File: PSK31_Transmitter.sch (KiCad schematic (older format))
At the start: 38 parts

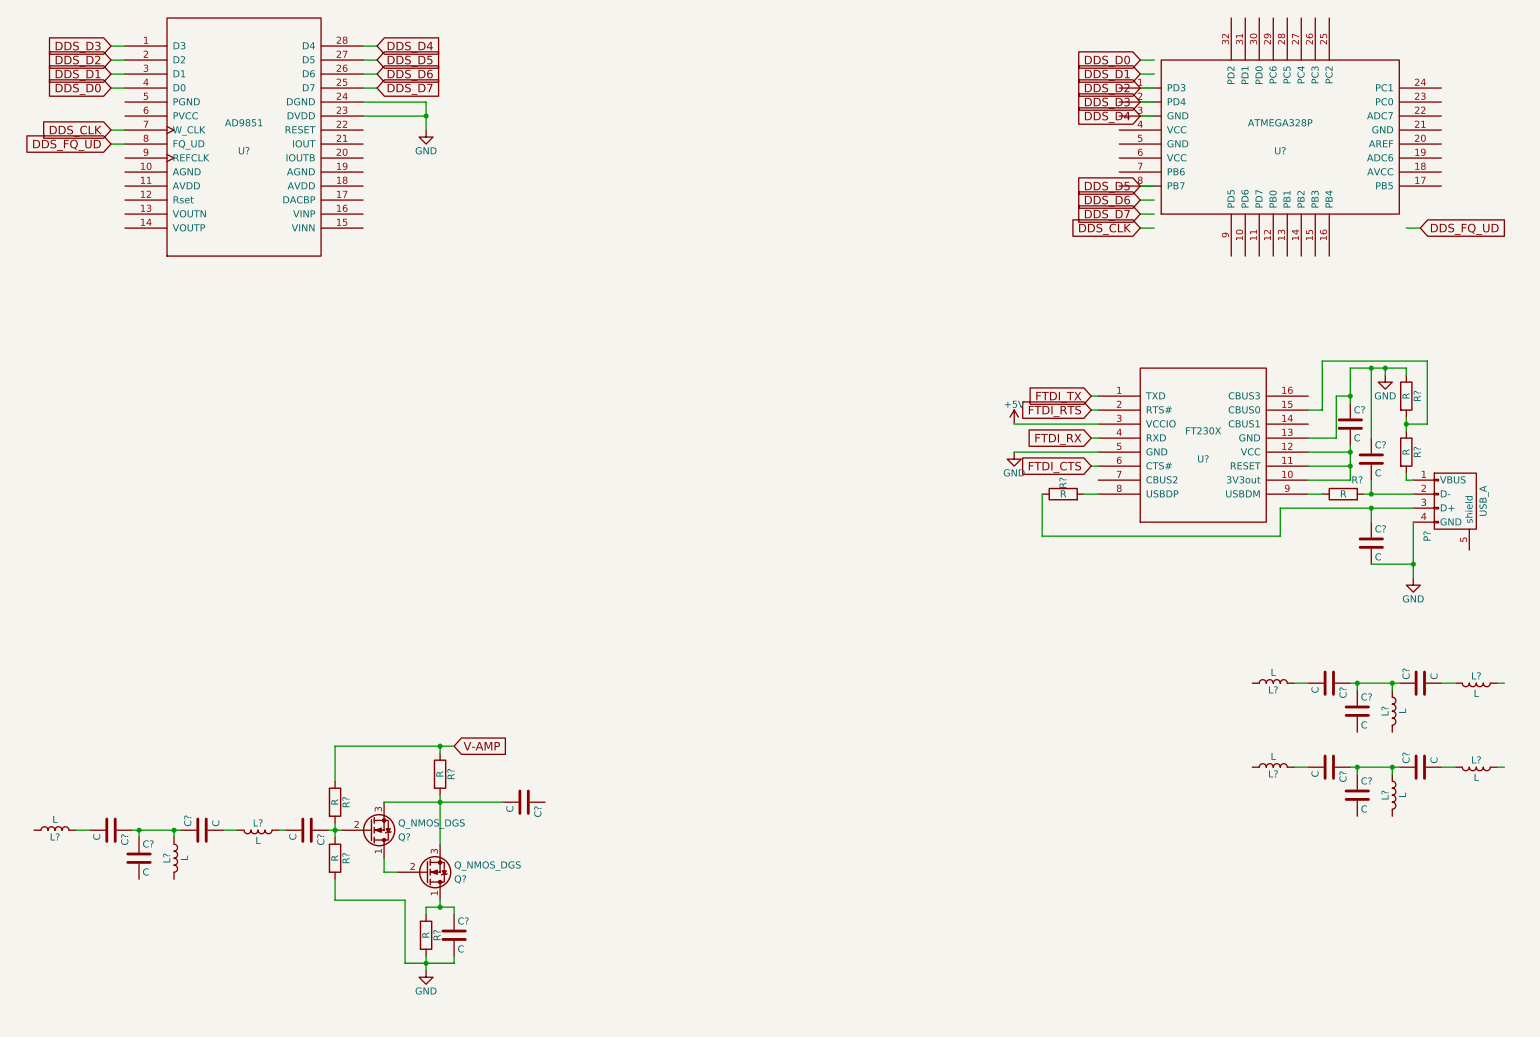
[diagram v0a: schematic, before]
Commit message: Add external circuitry for ftdi and dds.
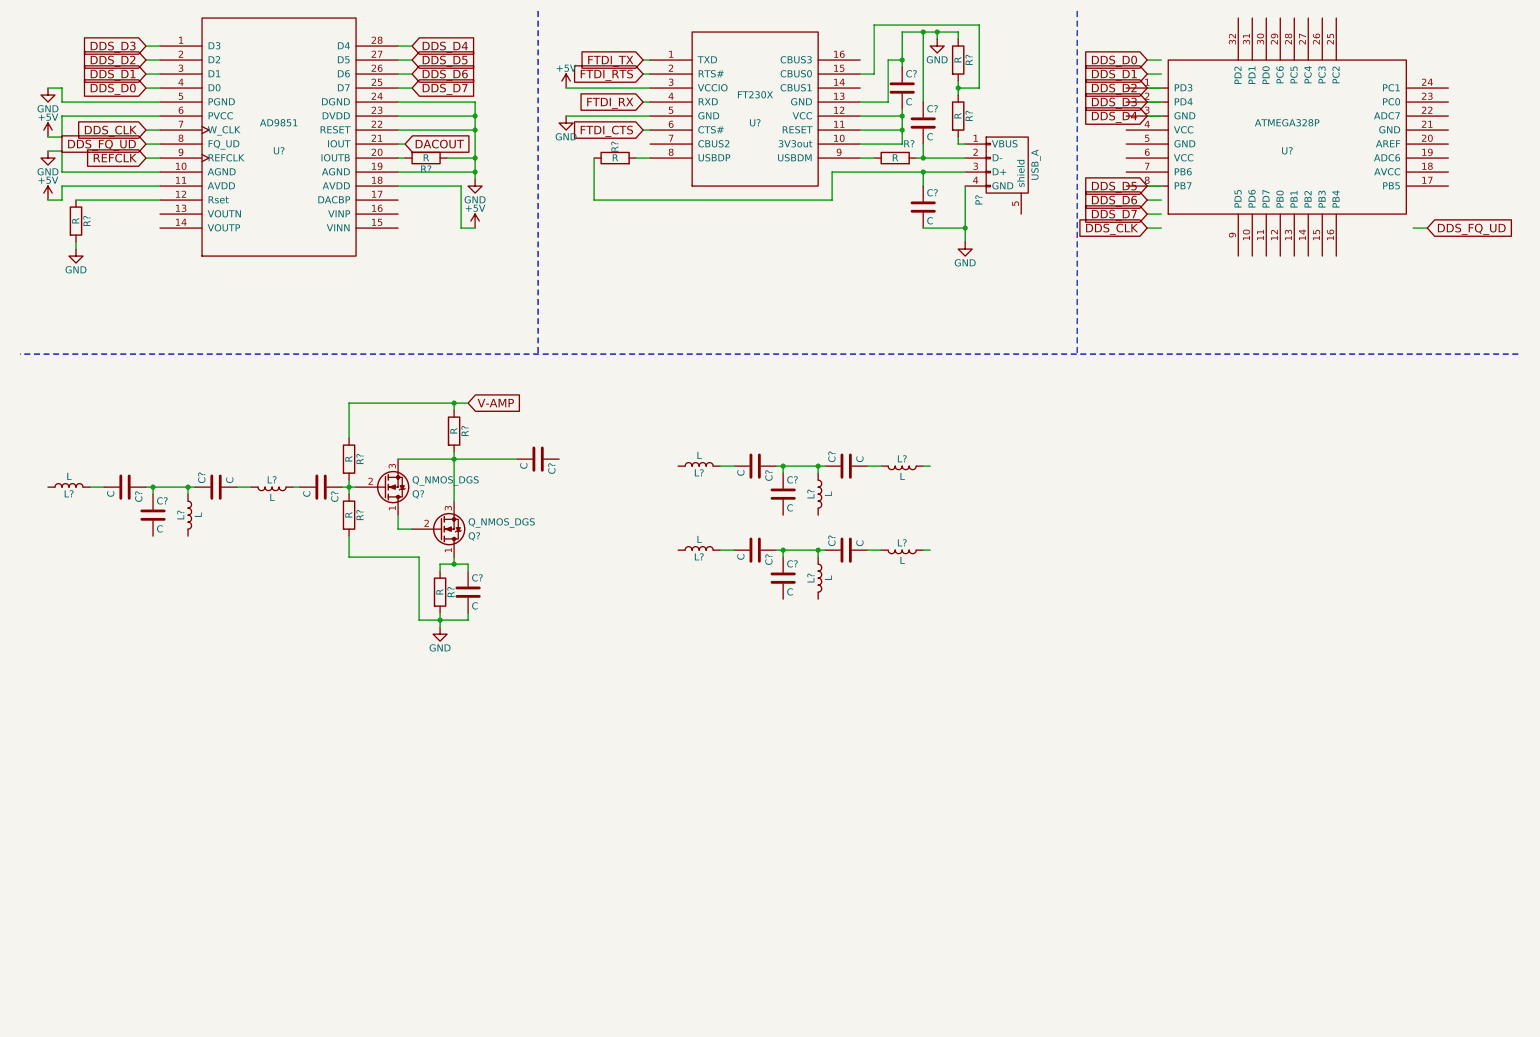
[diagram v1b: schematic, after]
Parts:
- added R? (x2): R, symbol R
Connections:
- net labels added: DACOUT, REFCLK
- wire segments 97 -> 120
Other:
- moved on the sheet: C?, L?, P?, Q?, R?, U?

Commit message: Add dac filter and dds reference clock
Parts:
- removed C? (x12): C, symbol C
- removed L? (x9): L, symbol L
- removed Q? (x2): Q_NMOS_DGS, symbol Q_NMOS_DGS
- removed R? (x4): R, symbol R
- added C? (x16): C, symbol C
- added L? (x4): L, symbol L
- added P?: CONN_01X02, symbol CONN_01X02
- added R?: R, symbol R
- added U?: TXETDDSANF-30.000000, MODULE, symbol TXETDDSANF-30.000000
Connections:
- net labels added: ISP_CLK, ISP_MISO, ISP_MOSI, ISP_RESET, RFOUT
- net labels removed: V-AMP
- wire segments 120 -> 128

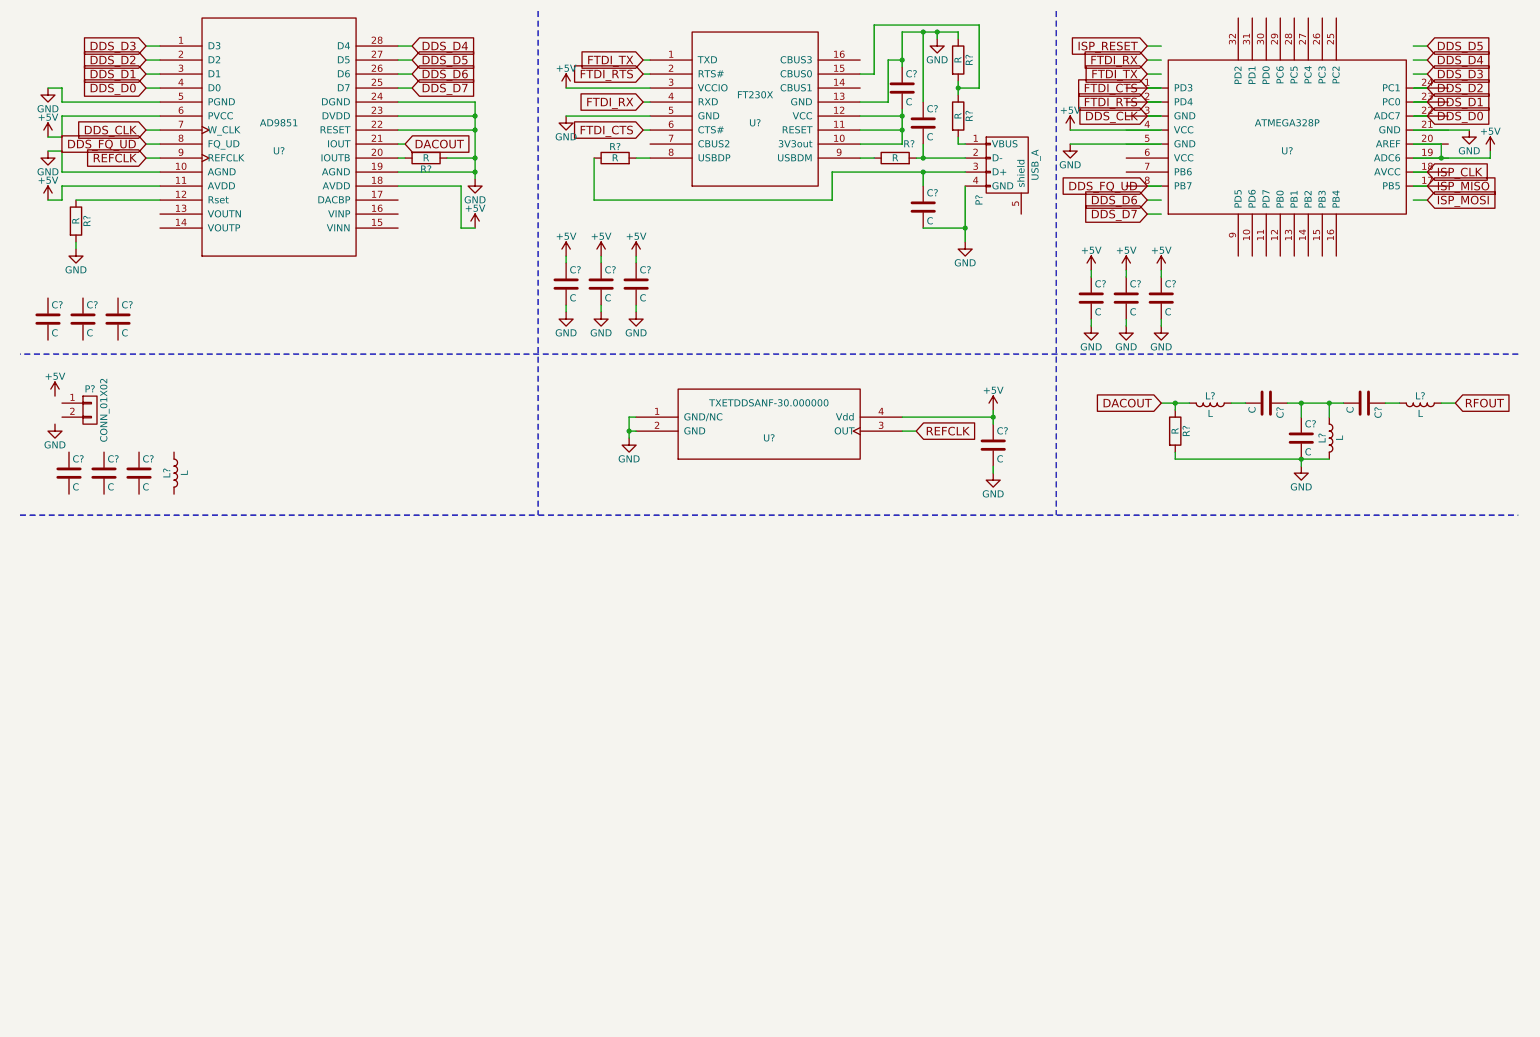
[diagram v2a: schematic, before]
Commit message: Add dds clock amplifer/filter and add dds output amplifier/filter
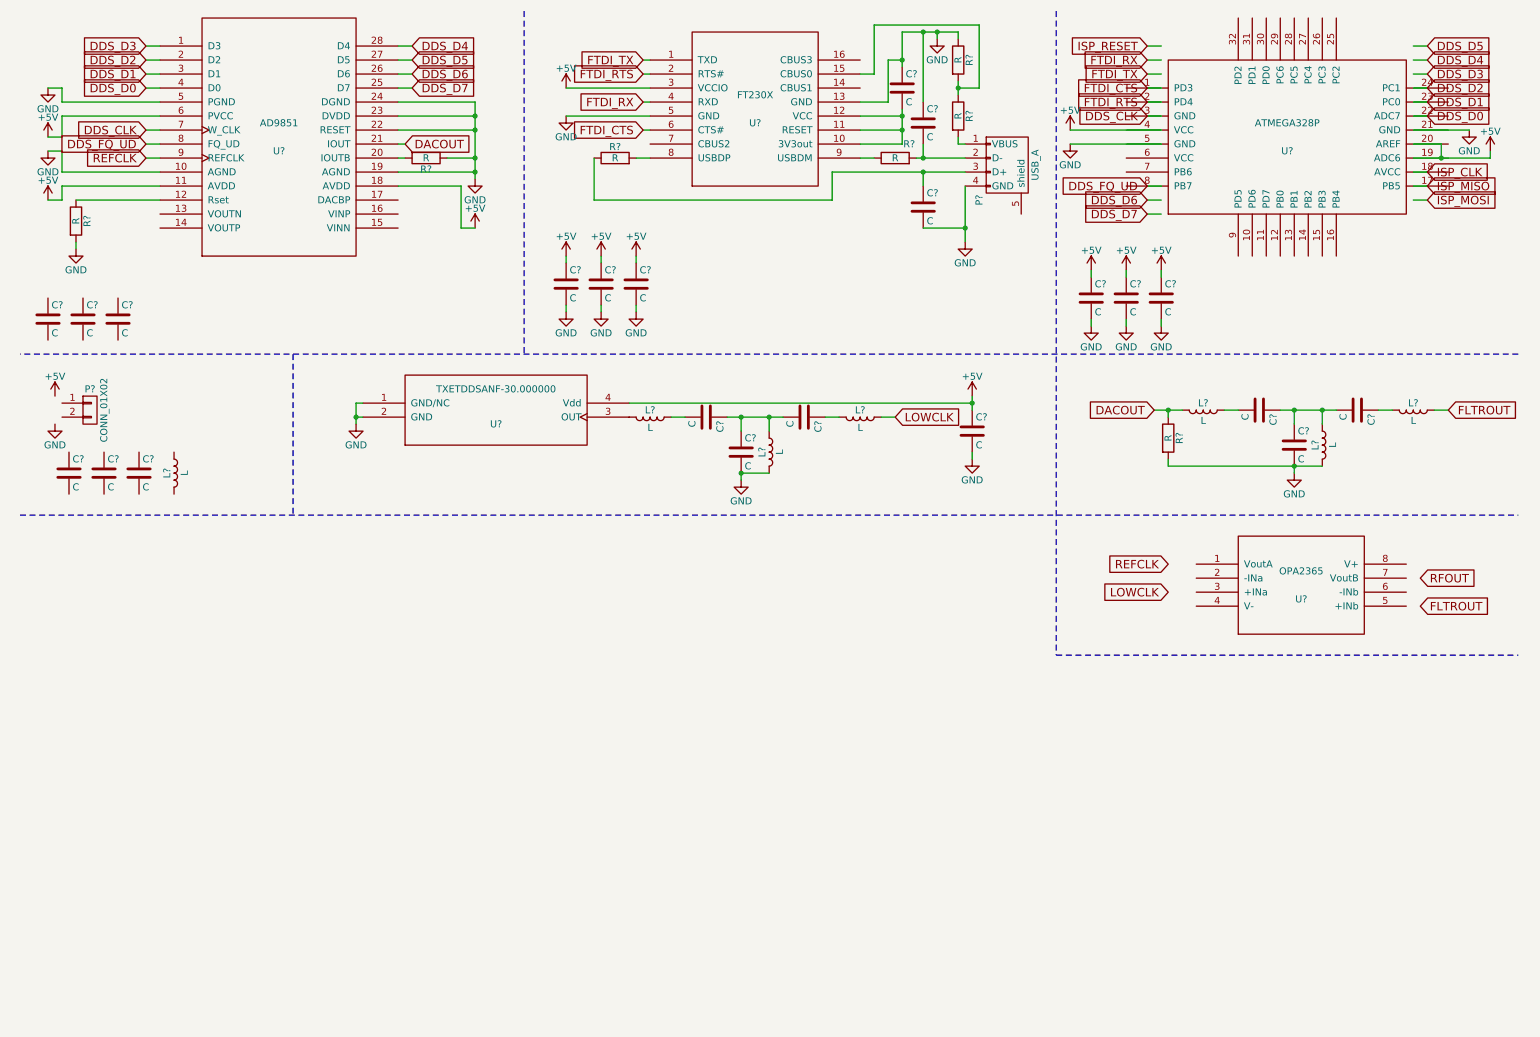
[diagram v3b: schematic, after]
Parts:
- added C? (x3): C, symbol C
- added L? (x3): L, symbol L
- added U?: OPA2365, MODULE, symbol OPA2365
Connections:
- net labels added: FLTROUT, LOWCLK
- wire segments 128 -> 135
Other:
- moved on the sheet: C?, L?, R?, U?

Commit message: update
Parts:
- removed C? (x19): C, symbol C
- removed L? (x7): L, symbol L
- removed P?: USB_A, symbol USB_A
- removed P?: CONN_01X02, symbol CONN_01X02
- removed R? (x5): R, symbol R
- removed U?: ATMEGA328P, MODULE, symbol ATMEGA328P
- removed U?: FT230X, MODULE, symbol FT230X
- added C1, C10, C11, C12, C13, C14, C16, C17, C19, C2, C21, C22, C23, C24, C25, C26, C27, C28, C29, C3, C30, C31, C32, C33, C4, C5, C6, C7, C8, C9: C, Capacitors_SMD:C_1206_HandSoldering, symbol C
- added L1, L2, L3, L4, L5, L6: L, Inductors_SMD:L_1206_Handsoldering, symbol L
- added P1: CONN_02X03, Pin_Headers:Pin_Header_Angled_2x03_Pitch2.54mm, symbol CONN_02X03
- added P2: CONN_01X04, Pin_Headers:Pin_Header_Angled_1x04_Pitch2.54mm, symbol CONN_01X04
- added P3: USB_A, Connectors:USB_A, symbol USB_A
- added P4: CONN_01X02, footprints:UMC, symbol CONN_01X02
- added P5: CONN_01X03, Pin_Headers:Pin_Header_Angled_1x03_Pitch2.54mm, symbol CONN_01X03
- added R2, R3, R5, R6, R7: R, Resistors_SMD:R_1206_HandSoldering, symbol R
- added U2: ATMEGA328P, Housings_QFP:TQFP-32_7x7mm_Pitch0.8mm, symbol ATMEGA328P
- added U4: FT232R, Housings_SSOP:SSOP-28_5.3x10.2mm_Pitch0.65mm, symbol FT232R
- C15, C18, C20: renamed from C?; footprint (none) -> Capacitors_SMD:C_1206_HandSoldering
- R1, R4: renamed from R?; footprint (none) -> Resistors_SMD:R_1206_HandSoldering
- U1: renamed from U?; footprint MODULE -> Housings_SSOP:SSOP-28_5.3x10.2mm_Pitch0.65mm
- U3: renamed from U?; footprint MODULE -> Housings_SOIC:SOIC-8_3.9x4.9mm_Pitch1.27mm
- U5: renamed from U?; footprint MODULE -> Oscillators:Oscillator_SMD_TXC_7C-4pin_5.0x3.2mm_HandSoldering
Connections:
- net labels added: +3.3V, ALG_SCL, ALG_SDA, DDS_REST, HICLK, ISP_REST, ISP_SCK, RAWCLK, USB_CTS, USB_DTR, USB_RX, USB_TX
- net labels removed: FLTROUT, FTDI_CTS, FTDI_RTS, FTDI_RX, FTDI_TX, ISP_CLK, ISP_RESET, RFOUT
- wire segments 135 -> 227
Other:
- moved on the sheet: C15, C18, C20, R1, R4, U1, U3, U5
